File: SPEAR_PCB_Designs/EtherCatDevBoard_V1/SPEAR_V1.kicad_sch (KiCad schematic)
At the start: 0 parts

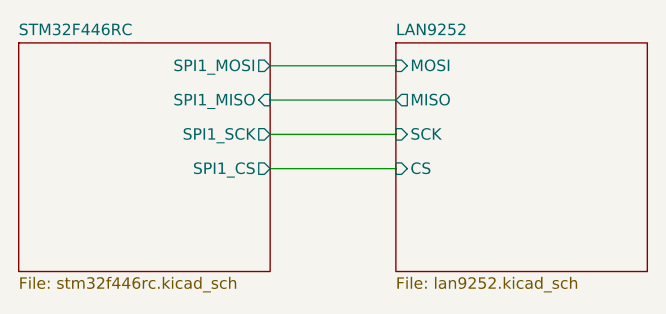
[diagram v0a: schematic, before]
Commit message: Continued work on EtherCAT microcontroller dev board. Updated it's head pinout.
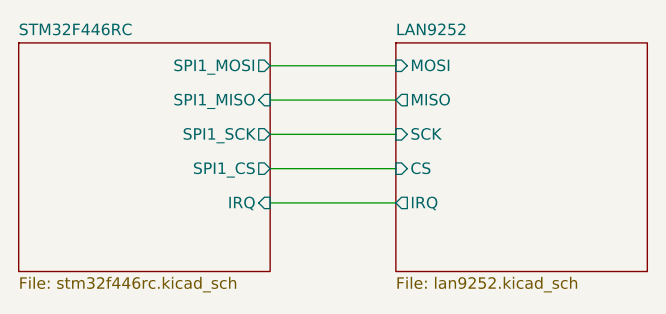
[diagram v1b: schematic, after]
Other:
- sheet LAN9252 ports: added IRQ; removed none
- sheet STM32F446RC ports: added IRQ; removed none
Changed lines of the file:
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@@
+	(wire
+		(pts
+			(xy 57.15 63.5) (xy 71.12 63.5)
+		)
+		(stroke
+			(width 0)
+			(type default)
+		)
+	)
 	(wire
 		(pts
@@
 			)
 		)
+		(pin "IRQ" input
+			(at 57.15 63.5 0)
+			(effects
+				(font
+					(size 1.27 1.27)
+				)
+				(justify right)
+			)
+		)
 		(instances
 			(project "SPEAR_V1"
@@
 			(effects
 				(font
+					(size 1.27 1.27)
+				)
+				(justify left)
+			)
+		)
+		(pin "IRQ" output
+			(at 71.12 63.5 180)
+			(effects
+				(font
